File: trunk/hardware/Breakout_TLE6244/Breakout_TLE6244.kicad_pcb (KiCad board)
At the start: 4 copper layers, 50.8 x 38.1 mm, 73 parts, among them K1 CONN_3, K2 CONN_3, K3 CONN_3, K4 CONN_3, K5 CONN_3, K6 CONN_3, K7 CONN_3, P1 CONN_4, P2 CONN_3, P3 CONN_2, P4 CONN_3, P5 CONN_5, P6 CONN_3, P7 CONN_2, P8 CONN_2, U1 TLE6244

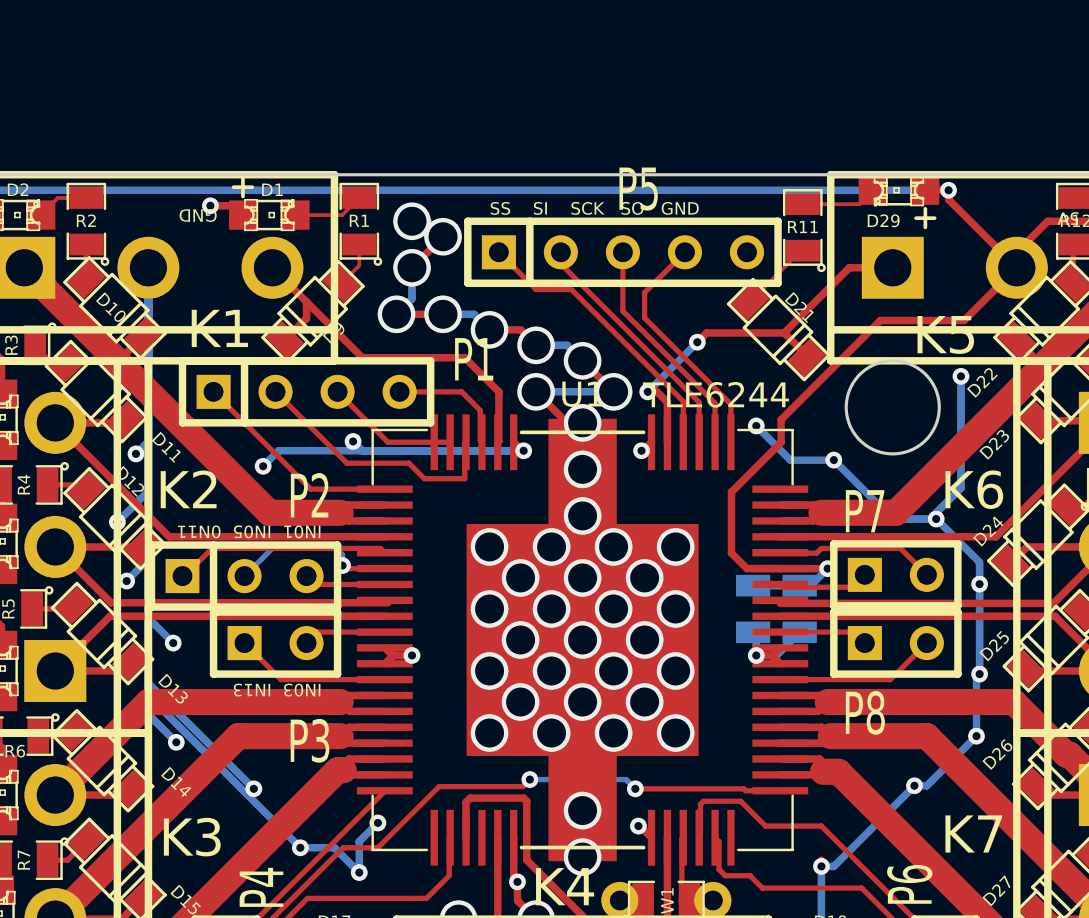
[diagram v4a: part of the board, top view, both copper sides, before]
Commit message: 
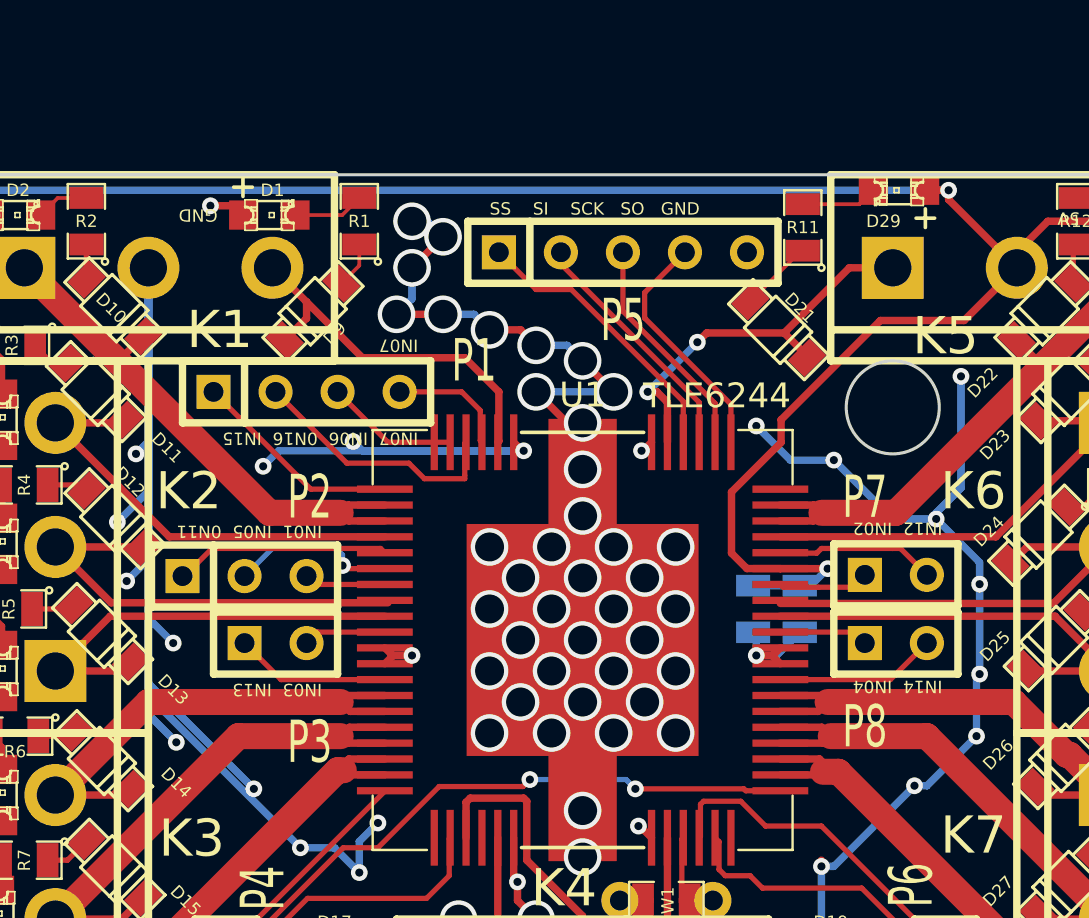
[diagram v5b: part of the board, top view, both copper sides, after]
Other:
- board text added: "IN07"
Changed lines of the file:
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@@
     (area 174.186532 113.03 264.160001 177.800001)
     (thickness 1.6)
-    (drawings 34)
+    (drawings 38)
     (tracks 617)
     (zones 0)
@@
       (drillshape 0)
       (scaleselection 1)
-      (outputdirectory frankenso_gerbers/))
+      (outputdirectory Breakout_TLE6244_gerbers/))
   )
   (net 0 "")
@@
     (descr "Connecteur 5 pins")
     (tags "CONN DEV")
-    (fp_text reference P5 (at -0.635 -2.54) (layer F.SilkS)
+    (fp_text reference P5 (at -1.27 2.794) (layer F.SilkS)
       (effects (font (size 1.72974 1.08712) (thickness 0.3048)))
     )
@@
     (descr "Connecteurs 2 pins")
     (tags "CONN DEV")
-    (fp_text reference P8 (at -1.27 2.921) (layer F.SilkS)
+    (fp_text reference P8 (at -1.27 3.429) (layer F.SilkS)
       (effects (font (size 1.72974 1.08712) (thickness 0.3048)))
     )
@@
     (descr "Connecteurs 2 pins")
     (tags "CONN DEV")
-    (fp_text reference P7 (at -1.27 -2.54) (layer F.SilkS)
+    (fp_text reference P7 (at -1.27 -3.175) (layer F.SilkS)
       (effects (font (size 1.72974 1.08712) (thickness 0.3048)))
     )
@@
     )
   )
+  (gr_text "IN12  IN02" (at 240.792 144.018 180) (layer F.SilkS)
+    (effects (font (size 0.508 0.508) (thickness 0.127)) (justify left))
+  )
+  (gr_text "IN14  IN04" (at 240.792 150.495 180) (layer F.SilkS)
+    (effects (font (size 0.508 0.508) (thickness 0.127)) (justify left))
+  )
+  (gr_text IN07 (at 219.329 136.525 180) (layer F.SilkS)
+    (effects (font (size 0.508 0.508) (thickness 0.127)) (justify left))
+  )
+  (gr_text "IN07  IN06  0N16  IN15" (at 219.329 140.335 180) (layer F.SilkS)
+    (effects (font (size 0.508 0.508) (thickness 0.127)) (justify left))
+  )
   (gr_text "             5V            " (at 249.301 131.318 180) (layer F.SilkS)
     (effects (font (size 0.508 0.508) (thickness 0.127)) (justify left))
@@
   (via (at 220.98 160.02) (size 1.54178) (drill 1.18618) (layers F.Cu B.Cu) (net 44))
   (segment (start 222.885 161.925) (end 220.98 160.02) (width 0.3048) (layer B.Cu) (net 44))
-  (segment (start 227.584 159.258) (end 227.584 161.544) (width 0.3048) (layer F.Cu) (net 44) (status 400000))
+  (segment (start 227.584 159.258) (end 227.584 161.544) (width 0.3048) (layer F.Cu) (net 44))
   (via (at 228.6 165.735) (size 1.54178) (drill 1.18618) (layers F.Cu B.Cu) (net 44))
   (segment (start 228.6 163.83) (end 228.6 165.735) (width 0.3048) (layer F.Cu) (net 44))
@@
   (via (at 224.155 160.02) (size 1.54178) (drill 1.18618) (layers F.Cu B.Cu) (net 44))
   (segment (start 223.393 159.258) (end 224.155 160.02) (width 0.3048) (layer F.Cu) (net 44))
-  (segment (start 226.06 141.732) (end 226.06 140.335) (width 0.3048) (layer F.Cu) (net 44) (status C00000))
+  (segment (start 226.06 141.732) (end 226.06 140.335) (width 0.3048) (layer F.Cu) (net 44))
   (via (at 219.075 131.445) (size 1.54178) (drill 1.18618) (layers F.Cu B.Cu) (net 44))
   (segment (start 219.71 131.445) (end 219.075 131.445) (width 0.3048) (layer B.Cu) (net 44))
@@
   (segment (start 224.155 138.43) (end 227.33 138.43) (width 0.3048) (layer B.Cu) (net 44))
   (via (at 224.155 138.43) (size 1.54178) (drill 1.18618) (layers F.Cu B.Cu) (net 44))
-  (segment (start 226.06 140.335) (end 224.155 138.43) (width 0.3048) (layer F.Cu) (net 44) (status 400000))
+  (segment (start 226.06 140.335) (end 224.155 138.43) (width 0.3048) (layer F.Cu) (net 44))
   (segment (start 226.06 148.59) (end 226.06 155.575) (width 0.3048) (layer F.Cu) (net 44))
   (segment (start 226.06 157.48) (end 226.06 155.448) (width 0.3048) (layer F.Cu) (net 44))
